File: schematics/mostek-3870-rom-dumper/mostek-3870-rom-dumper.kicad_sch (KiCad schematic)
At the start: 10 parts

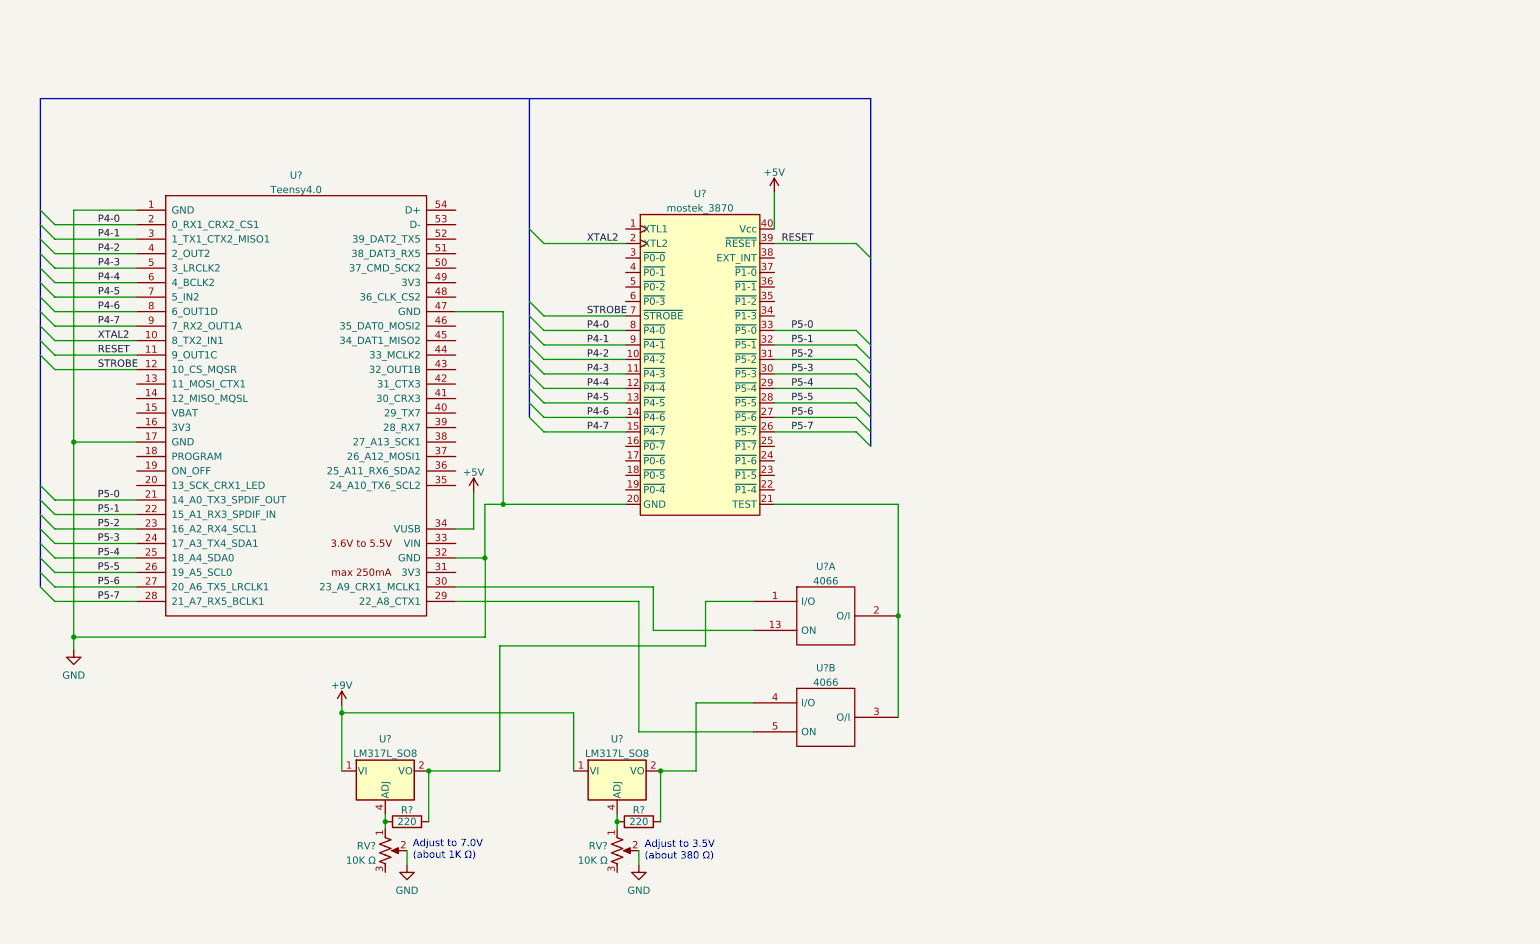
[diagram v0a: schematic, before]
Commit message: updated design to using an ATMEGA1284P
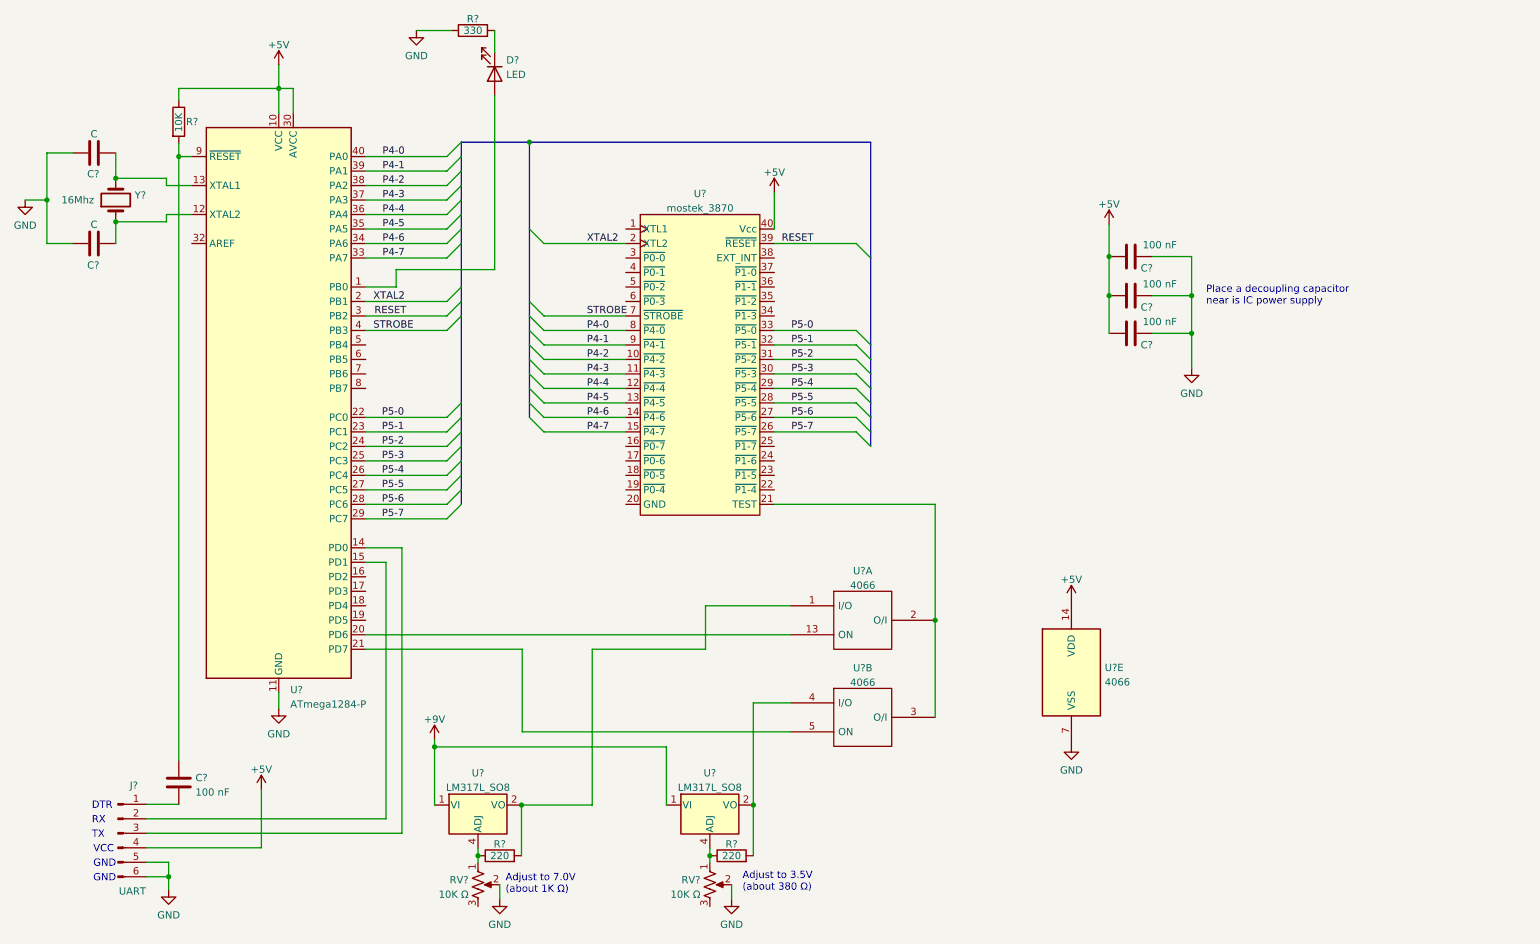
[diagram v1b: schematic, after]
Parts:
- removed U?: Teensy4.0, symbol teensy:Teensy4.0
- added C? (x2): C, symbol Device:C
- added C? (x4): 100 nF, symbol Device:C
- added D?: LED, symbol Device:LED
- added J?: UART, symbol Connector:Conn_01x06_Male
- added R?: 330, symbol Device:R
- added R?: 10K, symbol Device:R
- added U?: ATmega1284-P, Package_DIP:DIP-40_W15.24mm, symbol MCU_Microchip_ATmega:ATmega1284-P
- added U?: 4066, symbol 4xxx:4066
- added Y?: 16Mhz, symbol Device:Crystal
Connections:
- net +5V: now also C?.1, C?.1, C?.1, J?.4 (Pin_4), R?.1, U?.10 (VCC), U?.14 (VDD), U?.30 (AVCC)
- net GND: now also C?.2, C?.2, C?.2, C?.2, C?.2, J?.5 (Pin_5), J?.6 (Pin_6), R?.1, U?.11 (GND), U?.31 (GND), U?.7 (VSS); no longer U?.20 (GND)
- net P4-0: now also U?.40 (PA0)
- net P4-1: now also U?.39 (PA1)
- net P4-2: now also U?.38 (PA2)
- net P4-3: now also U?.37 (PA3)
- net P4-4: now also U?.36 (PA4)
- net P4-5: now also U?.35 (PA5)
- net P4-6: now also U?.34 (PA6)
- net P4-7: now also U?.33 (PA7)
- net P5-0: now also U?.22 (PC0)
- net P5-1: now also U?.23 (PC1)
- net P5-2: now also U?.24 (PC2)
- net P5-3: now also U?.25 (PC3)
- net P5-4: now also U?.26 (PC4)
- net P5-5: now also U?.27 (PC5)
- net P5-6: now also U?.28 (PC6)
- net P5-7: now also U?.29 (PC7)
- net RESET: now also U?.3 (PB2)
- net STROBE: now also U?.4 (PB3)
- net XTAL2: now also U?.2 (PB1)
- net at U?.5 (ON): now also U?.21 (PD7)
- net at U?.13 (ON): now also U?.20 (PD6)
- new net: C?.1, U?.13 (XTAL1), Y?.2
- new net: D?.2 (A), U?.1 (PB0)
- new net: C?.1, U?.12 (XTAL2), Y?.1
- new net: J?.3 (Pin_3), U?.14 (PD0)
- new net: J?.2 (Pin_2), U?.15 (PD1)
- new net: C?.1, R?.2, U?.9 (~{RESET})
- new net: C?.2, J?.1 (Pin_1)
- new net: D?.1 (K), R?.2
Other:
- note added: "DTR"
- note added: "GND"
- note added: "Place a decoupling capacitor near is IC power supply"
- note added: "RX"
- note added: "TX"
- note added: "VCC"
- moved on the sheet: R?, RV?, U?, U?A, U?B

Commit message: working design cand code for ROM dumper
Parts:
- removed U?: LM317L_SO8, Package_SO:SOIC-8_3.9x4.9mm_P1.27mm, symbol Regulator_Linear:LM317L_SO8
- added R?: 220, symbol Device:R
- added R?: 10K, symbol Device:R
- added RV?: 10K Ω, symbol Device:R_Potentiometer_US
- added U? (x2): LM317, Package_TO_SOT_THT:TO-92_Inline, symbol Regulator_Linear:LM317L_TO92
- U?: value LM317L_SO8 -> LM317; footprint Package_SO:SOIC-8_3.9x4.9mm_P1.27mm -> Package_TO_SOT_THT:TO-92_Inline; symbol Regulator_Linear:LM317L_SO8 -> Regulator_Linear:LM317L_TO92
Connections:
- net +9V: now also U?.3 (VI), U?.3 (VI), U?.3 (VI); no longer U?.1 (VI)
- net GND: now also U?.20 (GND), U?.38 (EXT_INT), R?.2, RV?.2
- net at R?.2: now also U?.11 (I/O), U?.2 (VO); no longer U?.4 (I/O)
- net at R?.1, RV?.1: now also U?.1 (ADJ)
- net at U?.20 (PD6): now also U?.6 (ON); no longer U?.13 (ON)
- net at U?.21 (PD7): now also U?.12 (ON); no longer U?.5 (ON)
- net at R?.1, RV?.1: now also U?.1 (ADJ); no longer U?.4 (ADJ)
- net +5V renamed VCC
- net VCC: now also R?.2, U?.2 (VO); no longer J?.4 (Pin_4)
- new net: R?.1, RV?.1, U?.1 (ADJ)
- new net: R?.2, U?.2 (VO), U?.8 (I/O)
- new net: R?.1, U?.10 (O/I), U?.21 (TEST), U?.9 (O/I)
- no-connect marks 0 -> 1
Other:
- note added: "Adjust to 4.8V (about 620 ) The MK3870 performs best about 4.8V VCC. Otherwise it's Port 4 LOW values will be a little too high and occasionally be read as HIGH values by the ATMEGA1284P."
- note added: "The voltage from the tyupical UART is too high for the MK3870"
- moved on the sheet: C?

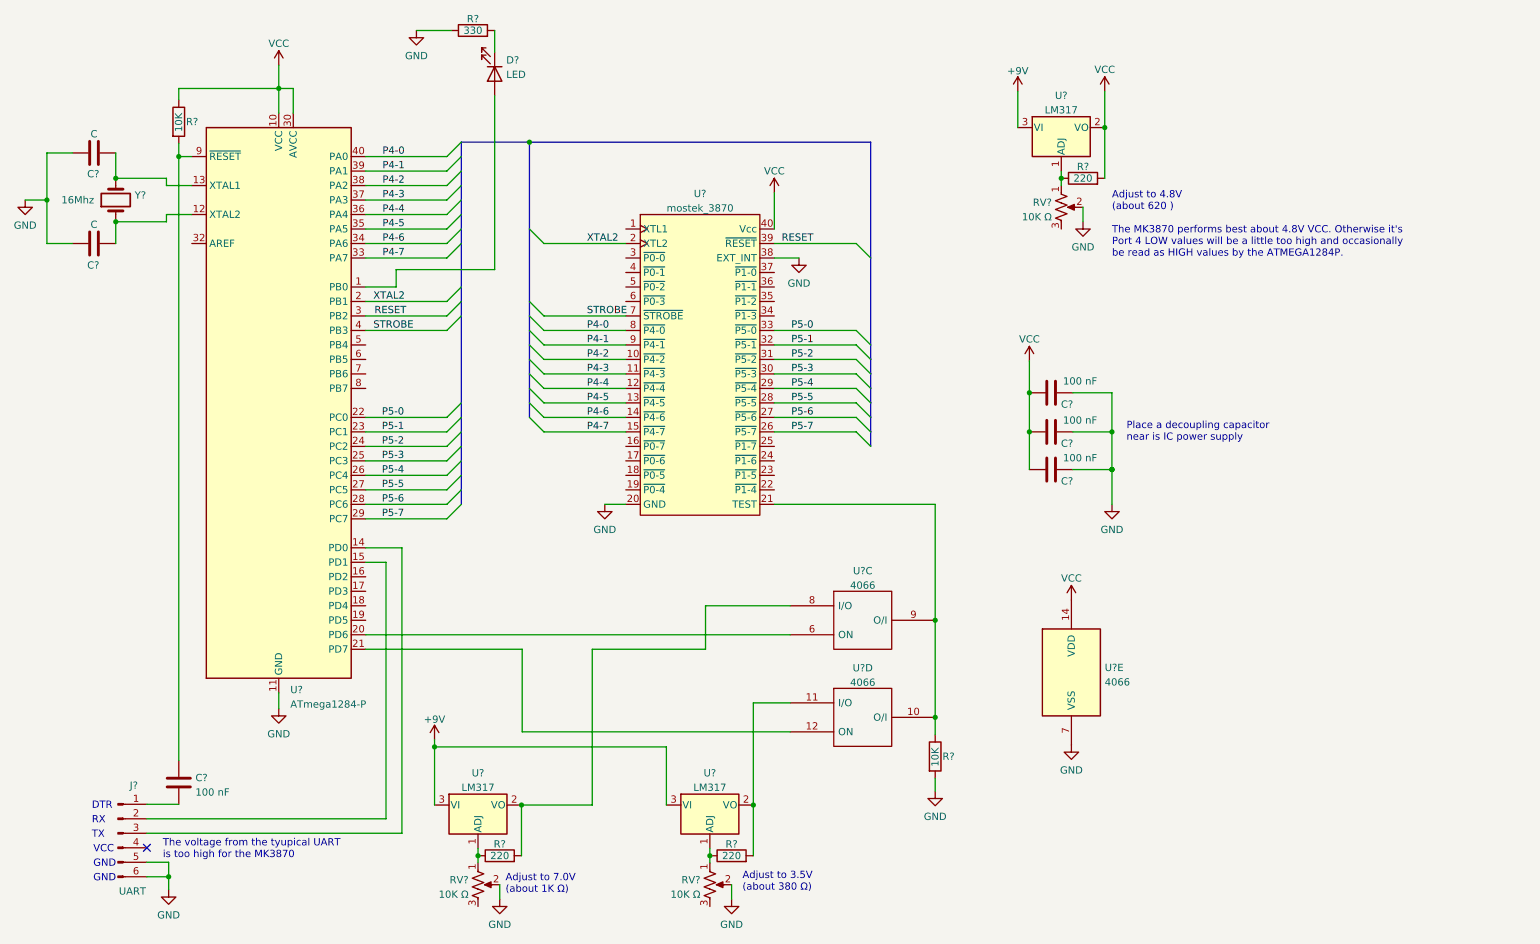
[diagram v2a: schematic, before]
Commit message: updated schematic notes
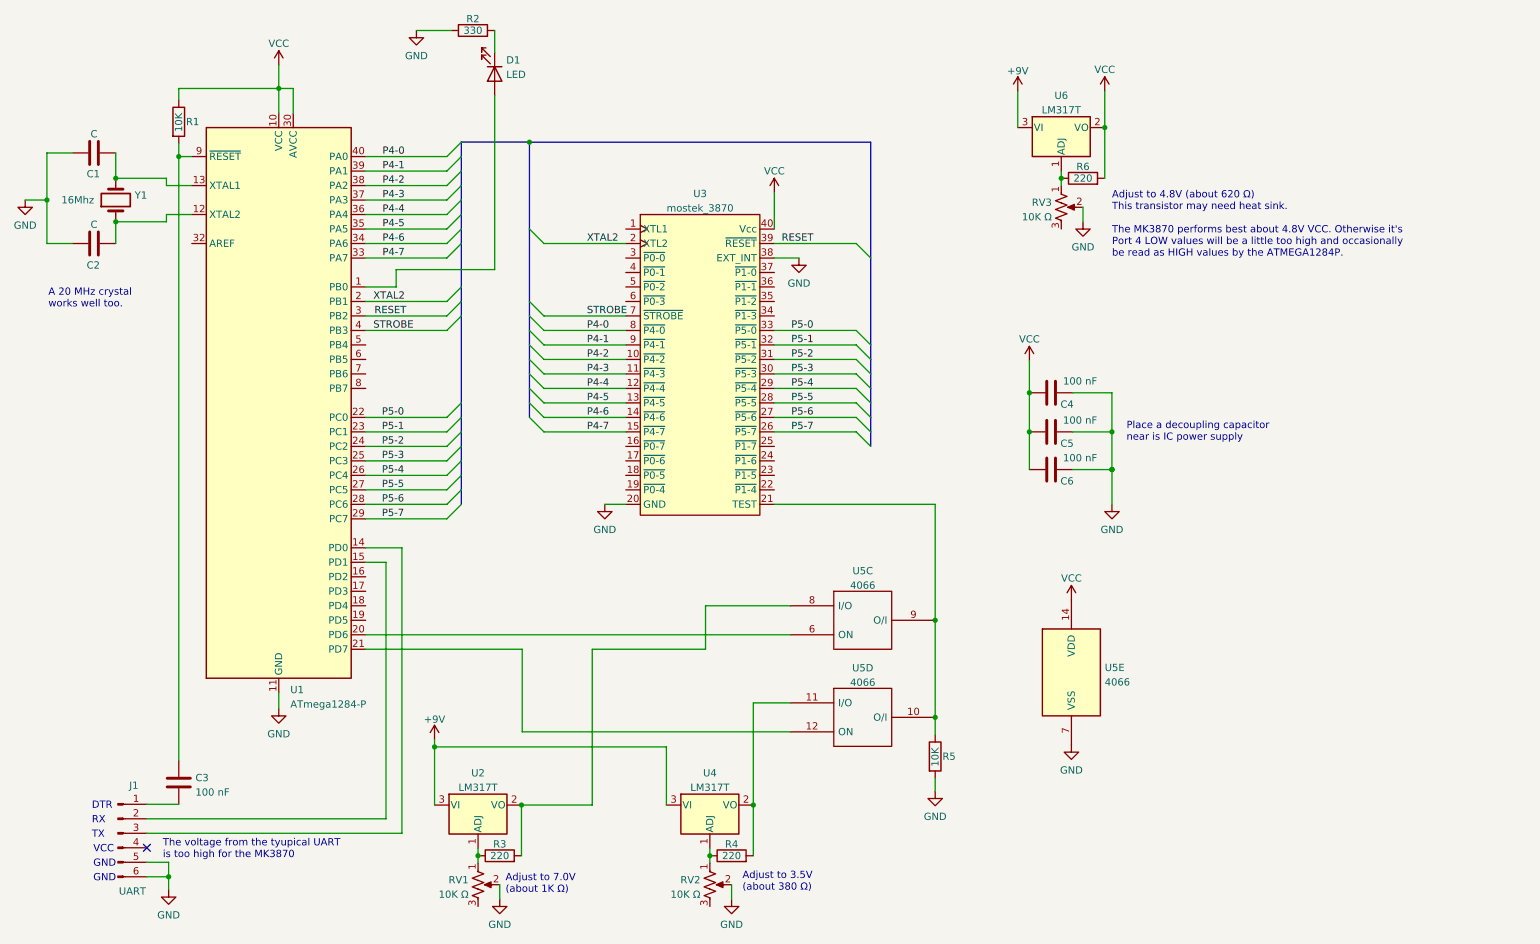
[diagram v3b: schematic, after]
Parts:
- U2, U4, U6: renamed from U?; value LM317 -> LM317T
- gave numbers to parts that had none: 21
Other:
- note added: "A 20 MHz crystal works well too."
- note added: "Adjust to 4.8V (about 620 Ω) This transistor may need heat sink. The MK3870 performs best about 4.8V VCC. Otherwise it's Port 4 LOW values will be a little too high and occasionally be read as HIGH values by the ATMEGA1284P."
- note removed: "Adjust to 4.8V (about 620 ) The MK3870 performs best about 4.8V VCC. Otherwise it's Port 4 LOW values will be a little too high and occasionally be read as HIGH values by the ATMEGA1284P."

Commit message: corrected 4066 power source
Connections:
- net +9V: now also U5.14 (VDD)
- net VCC: no longer U5.14 (VDD)
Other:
- note added: "The 4066 should be powered by the 9V source"
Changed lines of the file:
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@@
+    (effects (font (size 1.27 1.27)) (justify left bottom))
+  )
+  (text "The 4066 should be powered\nby the 9V source" (at 207.01 120.65 0)
     (effects (font (size 1.27 1.27)) (justify left bottom))
   )
@@
     (pin "2")
   )
-  (symbol (lib_id "power:VCC") (at 202.438 119.634 0) (unit 1)
-    (in_bom yes) (on_board yes)
-    (property "Reference" "#PWR0102" (id 0) (at 202.438 123.444 0)
-      (effects (font (size 1.27 1.27)) hide)
-    )
-    (property "Value" "VCC" (id 1) (at 202.438 115.824 0))
-    (property "Footprint" "" (id 2) (at 202.438 119.634 0)
-      (effects (font (size 1.27 1.27)) hide)
-    )
-    (property "Datasheet" "" (id 3) (at 202.438 119.634 0)
-      (effects (font (size 1.27 1.27)) hide)
-    )
-    (pin "1")
-  )
   (symbol (lib_id "power:VCC") (at 150.368 48.26 0) (unit 1)
     (in_bom yes) (on_board yes)
@@
     )
     (property "Datasheet" "" (id 3) (at 150.368 48.26 0)
+      (effects (font (size 1.27 1.27)) hide)
+    )
+    (pin "1")
+  )
+  (symbol (lib_id "power:+9V") (at 202.438 119.634 0) (unit 1)
+    (in_bom yes) (on_board yes) (fields_autoplaced)
+    (property "Reference" "#PWR?" (id 0) (at 202.438 123.444 0)
+      (effects (font (size 1.27 1.27)) hide)
+    )
+    (property "Value" "+9V" (id 1) (at 202.438 116.0582 0))
+    (property "Footprint" "" (id 2) (at 202.438 119.634 0)
+      (effects (font (size 1.27 1.27)) hide)
+    )
+    (property "Datasheet" "" (id 3) (at 202.438 119.634 0)
       (effects (font (size 1.27 1.27)) hide)
     )
@@
       (reference "#PWR0101") (unit 1) (value "GND") (footprint "")
     )
-    (path "/7468eaa7-1dfd-45de-8872-4aed59c3c0a3"
-      (reference "#PWR0102") (unit 1) (value "VCC") (footprint "")
-    )
     (path "/55404903-c030-44ad-b9e0-2d56116e36cc"
       (reference "#PWR0103") (unit 1) (value "GND") (footprint "")
@@
       (reference "#PWR0119") (unit 1) (value "GND") (footprint "")
     )
+    (path "/7d940308-7708-4193-803e-24eeb54c87f9"
+      (reference "#PWR?") (unit 1) (value "+9V") (footprint "")
+    )
     (path "/30092a32-fb53-42b0-ace5-6393064aca45"

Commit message: added MK3870 power control
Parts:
- added Q?: NDP6020P, symbol Transistor_FET:QM6015D
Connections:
- net VCC: now also Q?.3 (S); no longer U3.40 (Vcc)
- net at U1.19 (PD5): now also Q?.1 (G)
- new net: Q?.2 (D), U3.40 (Vcc)
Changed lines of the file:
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@@
+    (stroke (width 0) (type default) (color 0 0 0 0))
+  )
+  (wire (pts (xy 103.886 123.19) (xy 103.886 36.576))
     (stroke (width 0) (type default) (color 0 0 0 0))
   )
@@
     (stroke (width 0) (type default) (color 0 0 0 0))
   )
+  (wire (pts (xy 78.74 123.19) (xy 103.886 123.19))
+    (stroke (width 0) (type default) (color 0 0 0 0))
+  )
   (wire (pts (xy 209.5415 83.312) (xy 209.5415 90.17))
     (stroke (width 0) (type default) (color 0 0 0 0))
@@
     (stroke (width 0) (type default) (color 0 0 0 0))
   )
+  (wire (pts (xy 150.368 34.544) (xy 150.368 54.61))
+    (stroke (width 0) (type default) (color 0 0 0 0))
+  )
   (bus (pts (xy 107.442 67.31) (xy 107.442 69.85))
     (stroke (width 0) (type default) (color 0 0 0 0))
@@
     (stroke (width 0) (type default) (color 0 0 0 0))
   )
+  (wire (pts (xy 142.748 36.576) (xy 142.748 29.464))
+    (stroke (width 0) (type default) (color 0 0 0 0))
+  )
   (wire (pts (xy 209.5415 96.774) (xy 209.55 96.774))
     (stroke (width 0) (type default) (color 0 0 0 0))
@@
     (stroke (width 0) (type default) (color 0 0 0 0))
   )
-  (wire (pts (xy 150.368 48.26) (xy 150.368 54.61))
-    (stroke (width 0) (type default) (color 0 0 0 0))
-  )
   (wire (pts (xy 109.982 85.09) (xy 124.333 85.09))
     (stroke (width 0) (type default) (color 0 0 0 0))
@@
   )
   (wire (pts (xy 22.86 41.275) (xy 22.86 49.53))
+    (stroke (width 0) (type default) (color 0 0 0 0))
+  )
+  (wire (pts (xy 103.886 36.576) (xy 142.748 36.576))
     (stroke (width 0) (type default) (color 0 0 0 0))
   )
@@
     (pin "2")
   )
+  (symbol (lib_id "Transistor_FET:QM6015D") (at 147.828 29.464 0) (mirror x) (unit 1)
+    (in_bom yes) (on_board yes) (fields_autoplaced)
+    (property "Reference" "Q?" (id 0) (at 153.67 28.1939 0)
+      (effects (font (size 1.27 1.27)) (justify left))
+    )
+    (property "Value" "NDP6020P" (id 1) (at 153.67 30.7339 0)
+      (effects (font (size 1.27 1.27)) (justify left))
+    )
+    (property "Footprint" "" (id 2) (at 152.908 27.559 0)
+      (effects (font (size 1.27 1.27) italic) (justify left) hide)
+    )
+    (property "Datasheet" "" (id 3) (at 147.828 29.464 90)
+      (effects (font (size 1.27 1.27)) (justify left) hide)
+    )
+    (pin "1")
+    (pin "2")
+    (pin "3")
+  )
   (symbol (lib_id "power:GND") (at 202.438 145.034 0) (unit 1)
     (in_bom yes) (on_board yes) (fields_autoplaced)
@@
     (pin "2")
   )
-  (symbol (lib_id "power:VCC") (at 150.368 48.26 0) (unit 1)
-    (in_bom yes) (on_board yes)
-    (property "Reference" "#PWR0106" (id 0) (at 150.368 52.07 0)
-      (effects (font (size 1.27 1.27)) hide)
-    )
-    (property "Value" "VCC" (id 1) (at 150.368 44.45 0))
-    (property "Footprint" "" (id 2) (at 150.368 48.26 0)
-      (effects (font (size 1.27 1.27)) hide)
-    )
-    (property "Datasheet" "" (id 3) (at 150.368 48.26 0)
+  (symbol (lib_id "power:VCC") (at 150.368 24.384 0) (unit 1)
+    (in_bom yes) (on_board yes)
+    (property "Reference" "#PWR0106" (id 0) (at 150.368 28.194 0)
+      (effects (font (size 1.27 1.27)) hide)
+    )
+    (property "Value" "VCC" (id 1) (at 150.368 20.574 0))
+    (property "Footprint" "" (id 2) (at 150.368 24.384 0)
+      (effects (font (size 1.27 1.27)) hide)
+    )
+    (property "Datasheet" "" (id 3) (at 150.368 24.384 0)
       (effects (font (size 1.27 1.27)) hide)
     )
@@
       (reference "J1") (unit 1) (value "UART") (footprint "")
     )
+    (path "/51f4a558-1980-44ec-8fcd-9ada9c7f2ea4"
+      (reference "Q?") (unit 1) (value "NDP6020P") (footprint "")
+    )
     (path "/b366db1c-6870-4c09-8a34-b7319f75d53f"

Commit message: improved documentation
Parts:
- gave numbers to parts that had none: 1
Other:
- note added: "This MOSFET controls when power is applied to the MK3870."
